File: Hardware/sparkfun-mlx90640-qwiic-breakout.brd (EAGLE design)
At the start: 25.4 x 25.4 mm, 38 parts, among them J3 PTH, U1 110DEG

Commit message: updating to kit package
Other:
- board text added: "v11"
- board text removed: "v10"
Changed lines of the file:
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@@
 <wire x1="25.4" y1="25.4" x2="0" y2="25.4" width="0.1524" layer="20"/>
 <wire x1="0" y1="25.4" x2="0" y2="0" width="0.1524" layer="20"/>
-<text x="25.2095" y="6.35" size="1.27" layer="16" font="vector" ratio="15" rot="SMR270" align="bottom-center">v10</text>
+<text x="25.2095" y="6.35" size="1.27" layer="16" font="vector" ratio="15" rot="SMR270" align="bottom-center">v11</text>
 <text x="24.13" y="-7.62" size="1.778" layer="51" font="vector" align="bottom-center">Jim Lindblom</text>
 <text x="22.86" y="-10.16" size="1.778" layer="51" font="vector" align="bottom-center">Andy England</text>

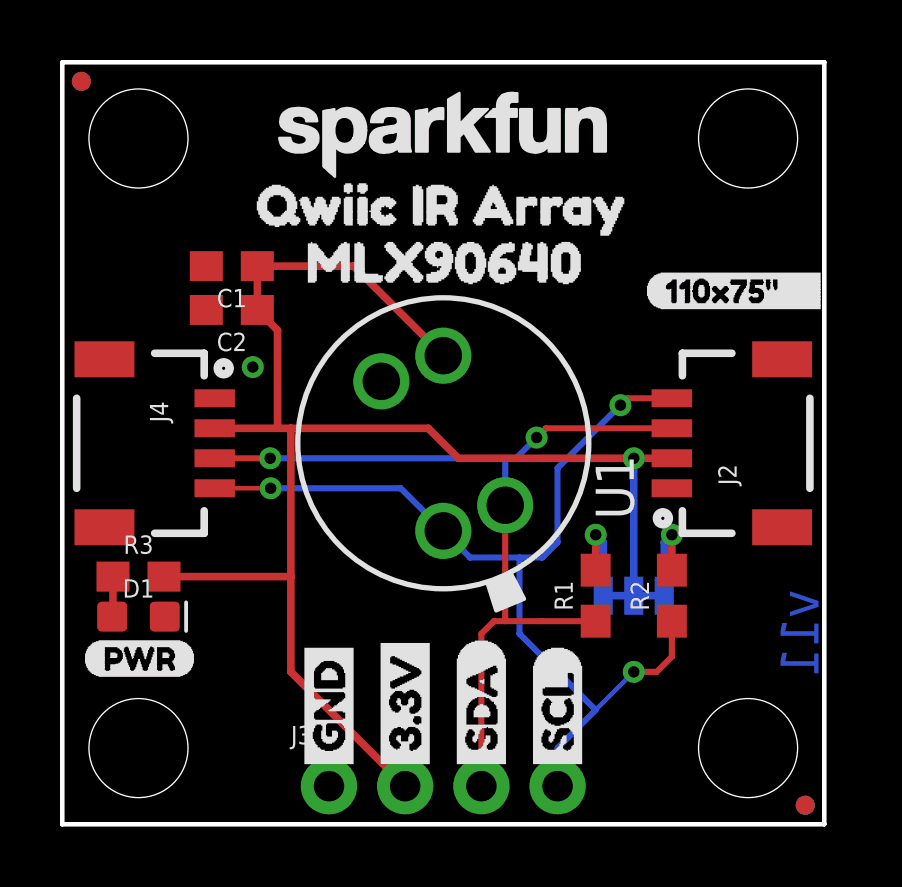
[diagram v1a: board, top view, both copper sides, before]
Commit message: fixing orientation
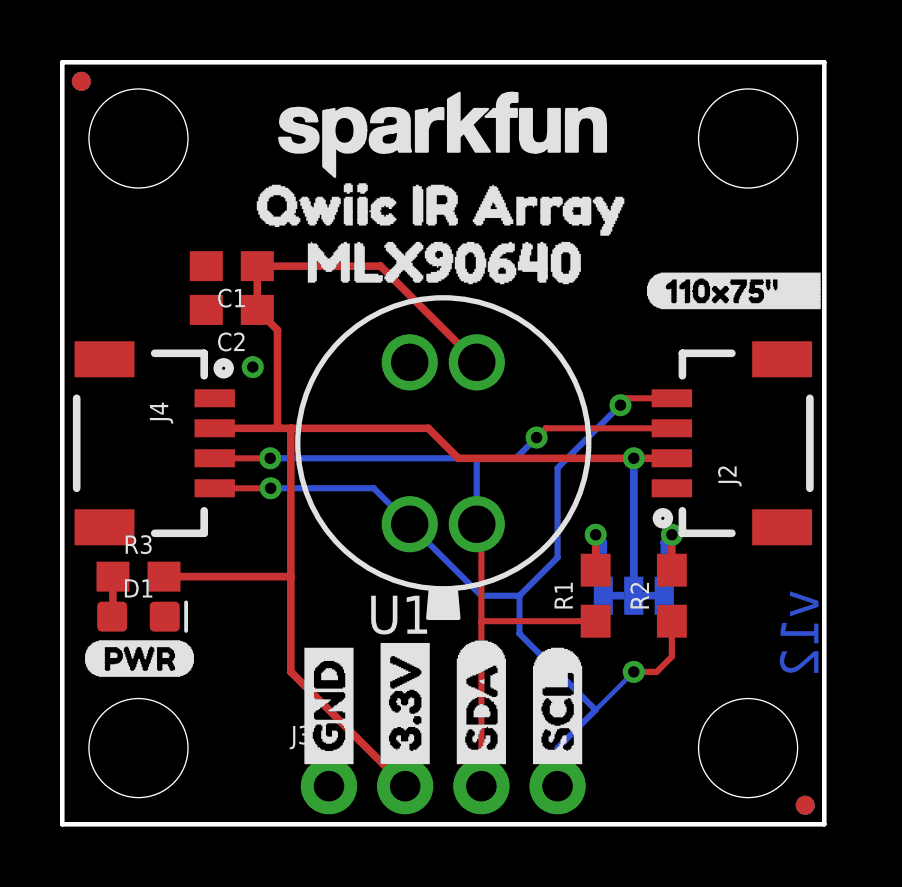
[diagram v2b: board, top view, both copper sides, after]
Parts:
- turned U1 to 0 degrees
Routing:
- net 3.3V: track 51.1 -> 52.3 mm
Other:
- board text added: "v12"
- board text removed: "v11"
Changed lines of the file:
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@@
 <wire x1="25.4" y1="25.4" x2="0" y2="25.4" width="0.1524" layer="20"/>
 <wire x1="0" y1="25.4" x2="0" y2="0" width="0.1524" layer="20"/>
-<text x="25.2095" y="6.35" size="1.27" layer="16" font="vector" ratio="15" rot="SMR270" align="bottom-center">v11</text>
+<text x="25.2095" y="6.35" size="1.27" layer="16" font="vector" ratio="15" rot="SMR270" align="bottom-center">v12</text>
 <text x="24.13" y="-7.62" size="1.778" layer="51" font="vector" align="bottom-center">Jim Lindblom</text>
 <text x="22.86" y="-10.16" size="1.778" layer="51" font="vector" align="bottom-center">Andy England</text>
@@
 <attribute name="PROD_ID" value="RES-07856" x="2.54" y="8.255" size="1.778" layer="27" display="off"/>
 </element>
-<element name="U1" library="SparkFun-IC-Special-Function" package="MLX90540_MLX90640" value="110DEG" x="12.7" y="12.7" rot="R90">
-<attribute name="PROD_ID" value="IC-14041" x="12.7" y="12.7" size="1.778" layer="27" rot="R90" display="off"/>
-<attribute name="VALUE" value="110DEG" x="12.7" y="12.7" size="1.778" layer="27" rot="R90" display="off"/>
+<element name="U1" library="SparkFun-IC-Special-Function" package="MLX90540_MLX90640" value="110DEG" x="12.7" y="12.7">
+<attribute name="PROD_ID" value="IC-14041" x="12.7" y="12.7" size="1.778" layer="27" display="off"/>
+<attribute name="VALUE" value="110DEG" x="12.7" y="12.7" size="1.778" layer="27" display="off"/>
 </element>
 <element name="JP3" library="SparkFun" package="STAND-OFF" value="STAND-OFF" x="2.54" y="22.86"/>
@@
 <wire x1="6.5015" y1="17.145" x2="7.1755" y2="16.471" width="0.254" layer="1"/>
 <wire x1="7.1755" y1="16.471" x2="7.1755" y2="13.2" width="0.254" layer="1"/>
-<wire x1="6.5015" y1="18.6055" x2="9.7145" y2="18.6055" width="0.254" layer="1"/>
-<wire x1="9.7145" y1="18.6055" x2="12.7" y2="15.62" width="0.254" layer="1"/>
 <wire x1="6.5015" y1="17.145" x2="6.5015" y2="18.6055" width="0.254" layer="1"/>
+<wire x1="10.609590625" y1="18.6055" x2="13.8174125" y2="15.397678125" width="0.254" layer="1"/>
+<wire x1="6.5015" y1="18.6055" x2="10.609590625" y2="18.6055" width="0.254" layer="1"/>
 </signal>
 <signal name="GND">
@@
 <contactref element="U1" pad="SCL"/>
 <contactref element="R2" pad="1"/>
-<wire x1="5.08" y1="11.2" x2="6.9455" y2="11.2" width="0.1524" layer="1"/>
+<wire x1="5.08" y1="11.2" x2="6.9455" y2="11.2" width="0.2032" layer="1"/>
 <via x="6.9455" y="11.2" extent="1-16" drill="0.381"/>
-<wire x1="6.9455" y1="11.2" x2="11.28" y2="11.2" width="0.2032" layer="16"/>
 <wire x1="20.32" y1="14.2" x2="18.8355" y2="14.2" width="0.2032" layer="1"/>
 <wire x1="18.8355" y1="14.2" x2="18.6055" y2="13.97" width="0.2032" layer="1"/>
 <via x="18.6055" y="13.97" extent="1-16" drill="0.381"/>
-<wire x1="11.28" y1="11.2" x2="12.7" y2="9.78" width="0.2032" layer="16"/>
-<wire x1="16.51" y1="11.8745" x2="18.6055" y2="13.97" width="0.2032" layer="16"/>
-<wire x1="13.59" y1="8.89" x2="12.7" y2="9.78" width="0.2032" layer="16"/>
-<wire x1="15.24" y1="8.89" x2="13.59" y2="8.89" width="0.2032" layer="16"/>
+<wire x1="18.6055" y1="13.97" x2="16.51" y2="11.8745" width="0.2032" layer="16"/>
 <wire x1="16.51" y1="1.27" x2="16.51" y2="2.54" width="0.2032" layer="16"/>
 <wire x1="16.51" y1="2.54" x2="17.78" y2="3.81" width="0.2032" layer="16"/>
 <via x="19.05" y="5.08" extent="1-16" drill="0.381"/>
 <wire x1="17.78" y1="3.81" x2="19.05" y2="5.08" width="0.1524" layer="16"/>
-<wire x1="15.24" y1="8.89" x2="15.24" y2="6.35" width="0.2032" layer="16"/>
+<wire x1="15.24" y1="7.62" x2="15.24" y2="6.35" width="0.2032" layer="16"/>
 <wire x1="15.24" y1="6.35" x2="17.78" y2="3.81" width="0.2032" layer="16"/>
-<wire x1="15.24" y1="8.89" x2="16.002" y2="8.89" width="0.2032" layer="16"/>
-<wire x1="16.002" y1="8.89" x2="16.51" y2="9.398" width="0.2032" layer="16"/>
-<wire x1="16.51" y1="9.398" x2="16.51" y2="11.8745" width="0.2032" layer="16"/>
 <wire x1="19.05" y1="5.08" x2="19.812" y2="5.08" width="0.2032" layer="1"/>
 <wire x1="19.812" y1="5.08" x2="20.32" y2="5.588" width="0.2032" layer="1"/>
 <wire x1="20.32" y1="5.588" x2="20.32" y2="6.77" width="0.2032" layer="1"/>
+<wire x1="6.9455" y1="11.2" x2="10.384909375" y2="11.2" width="0.2032" layer="16"/>
+<wire x1="10.384909375" y1="11.2" x2="11.5825875" y2="10.002321875" width="0.2032" layer="16"/>
+<wire x1="10.384909375" y1="11.2" x2="10.384909375" y2="11.2" width="0.2032" layer="16"/>
+<wire x1="16.51" y1="8.89" x2="15.24" y2="7.62" width="0.2032" layer="16"/>
+<wire x1="16.51" y1="11.8745" x2="16.51" y2="8.89" width="0.2032" layer="16"/>
+<wire x1="15.24" y1="7.62" x2="13.964909375" y2="7.62" width="0.2032" layer="16"/>
+<wire x1="13.964909375" y1="7.62" x2="11.5825875" y2="10.002321875" width="0.2032" layer="16"/>
 </signal>
 <signal name="SDA">
@@
 <wire x1="5.08" y1="12.2" x2="6.9295" y2="12.2" width="0.2032" layer="1"/>
 <via x="6.9295" y="12.2" extent="1-16" drill="0.381"/>
-<wire x1="6.9295" y1="12.2" x2="14.764753125" y2="12.2" width="0.2032" layer="16"/>
+<wire x1="6.9295" y1="12.2" x2="13.843" y2="12.2" width="0.2032" layer="16"/>
+<wire x1="13.843" y1="12.2" x2="14.764753125" y2="12.2" width="0.2032" layer="16"/>
 <wire x1="14.764753125" y1="12.2" x2="15.121" y2="12.2" width="0.2032" layer="16"/>
 <wire x1="20.32" y1="13.2" x2="16.121" y2="13.2" width="0.2032" layer="1"/>
@@
 <via x="15.8115" y="12.8905" extent="1-16" drill="0.381"/>
 <wire x1="15.121" y1="12.2" x2="15.8115" y2="12.8905" width="0.2032" layer="16"/>
-<wire x1="14.764753125" y1="10.635246875" x2="14.764753125" y2="12.2" width="0.2032" layer="16"/>
-<wire x1="17.78" y1="6.77" x2="15.99" y2="6.77" width="0.2032" layer="1"/>
-<wire x1="14.764753125" y1="7.384753125" x2="14.764753125" y2="10.635246875" width="0.2032" layer="1"/>
-<wire x1="15.99" y1="6.77" x2="14.76" y2="6.77" width="0.2032" layer="1"/>
-<wire x1="14.76" y1="6.77" x2="14.39" y2="6.77" width="0.2032" layer="1"/>
-<wire x1="14.39" y1="6.77" x2="13.97" y2="6.35" width="0.2032" layer="1"/>
-<wire x1="14.764753125" y1="7.384753125" x2="14.764753125" y2="6.774753125" width="0.2032" layer="1"/>
-<wire x1="14.764753125" y1="6.774753125" x2="14.76" y2="6.77" width="0.1524" layer="1"/>
-<wire x1="13.97" y1="6.35" x2="13.97" y2="1.27" width="0.2032" layer="1"/>
+<wire x1="13.81741875" y1="10.0023125" x2="13.81741875" y2="12.17441875" width="0.2032" layer="16"/>
+<wire x1="13.81741875" y1="12.17441875" x2="13.843" y2="12.2" width="0.1778" layer="16"/>
+<wire x1="13.97" y1="9.84973125" x2="13.81741875" y2="10.0023125" width="0.2032" layer="1"/>
+<wire x1="13.97" y1="1.27" x2="13.97" y2="6.731" width="0.2032" layer="1"/>
+<wire x1="13.97" y1="6.731" x2="13.97" y2="9.84973125" width="0.2032" layer="1"/>
+<wire x1="14.009" y1="6.77" x2="13.97" y2="6.731" width="0.2032" layer="1"/>
+<wire x1="17.78" y1="6.77" x2="14.009" y2="6.77" width="0.2032" layer="1"/>
 </signal>
 <signal name="N$1">

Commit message: Updating silk for single PCB design
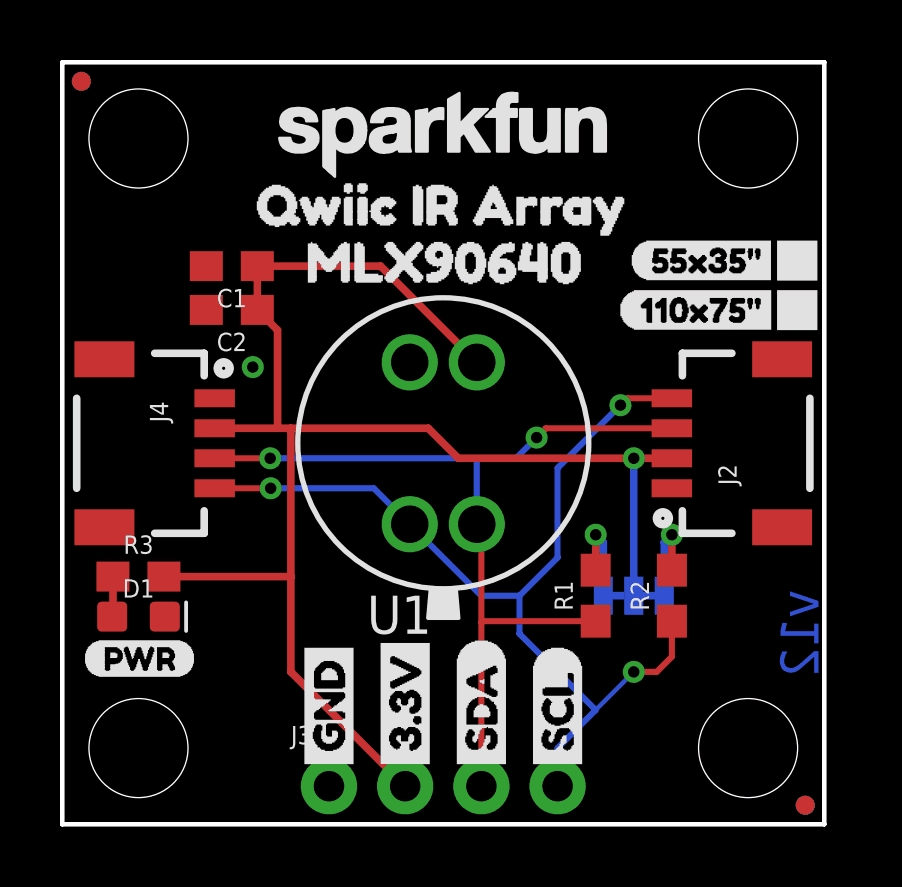
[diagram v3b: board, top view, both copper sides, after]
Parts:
- removed U$2: (no value), buzzard_labels (12):110X75#____0
- added U$15: (no value), buzzard_labels (9):110X75#0
- added U$3: (no value), buzzard_labels (9):55X35#1
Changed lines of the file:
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@@
 <setting verticaltext="up"/>
 </settings>
-<grid distance="0.05" unitdist="inch" unit="inch" style="lines" multiple="1" display="yes" altdistance="0.005" altunitdist="inch" altunit="inch"/>
+<grid distance="0.05" unitdist="inch" unit="inch" style="lines" multiple="1" display="yes" altdistance="0.0005" altunitdist="inch" altunit="inch"/>
 <layers>
 <layer number="1" name="Top" color="4" fill="1" visible="yes" active="yes"/>
@@
 <dimension x1="2.54" y1="22.86" x2="22.86" y2="22.86" x3="12.7" y3="27.06" textsize="1.778" layer="47" unit="inch"/>
 <text x="-13.53" y="25.83" size="1.778" layer="47" font="vector">Units in In.</text>
+<rectangle x1="23.8252" y1="18.1229" x2="25.1714" y2="19.4564" layer="21"/>
+<rectangle x1="23.8252" y1="16.4719" x2="25.1714" y2="17.8054" layer="21"/>
 </plain>
 <attributes>
@@
 <element name="LOGO4" library="SparkFun-Aesthetics" package="REVISION" value="REVISION" x="1.27" y="-10.16"/>
 <element name="LOGO3" library="SparkFun-Aesthetics" package="SFE_LOGO_NAME_.1" value="SFE_LOGO_NAME.1_INCH" x="6.731" y="21.082"/>
-<element name="U$2" library="buzzard_labels (12)" package="110X75#____0" value="" x="19.431" y="17.78"/>
+<element name="U$3" library="buzzard_labels (9)" package="55X35#1" value="" x="18.923" y="18.796"/>
+<element name="U$15" library="buzzard_labels (9)" package="110X75#0" value="" x="18.542" y="17.145"/>
 </elements>
 <signals>
